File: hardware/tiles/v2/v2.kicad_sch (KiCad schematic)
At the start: 24 parts, among them J1 Conn_01x05_Pin, J2 Conn_01x05_Pin, J3 Conn_01x05_Pin, J4 Conn_01x05_Pin, J5 Conn_01x05_Pin, J6 Conn_01x05_Pin, J7 Conn_01x05_Pin, J8 Conn_01x05_Pin, J9 Conn_01x06_Pin, SW1 SW_DIP_x01, U1 ATmega328P-A, U2 DRV5055A2xDBZxQ1, Y2 Crystal_GND24

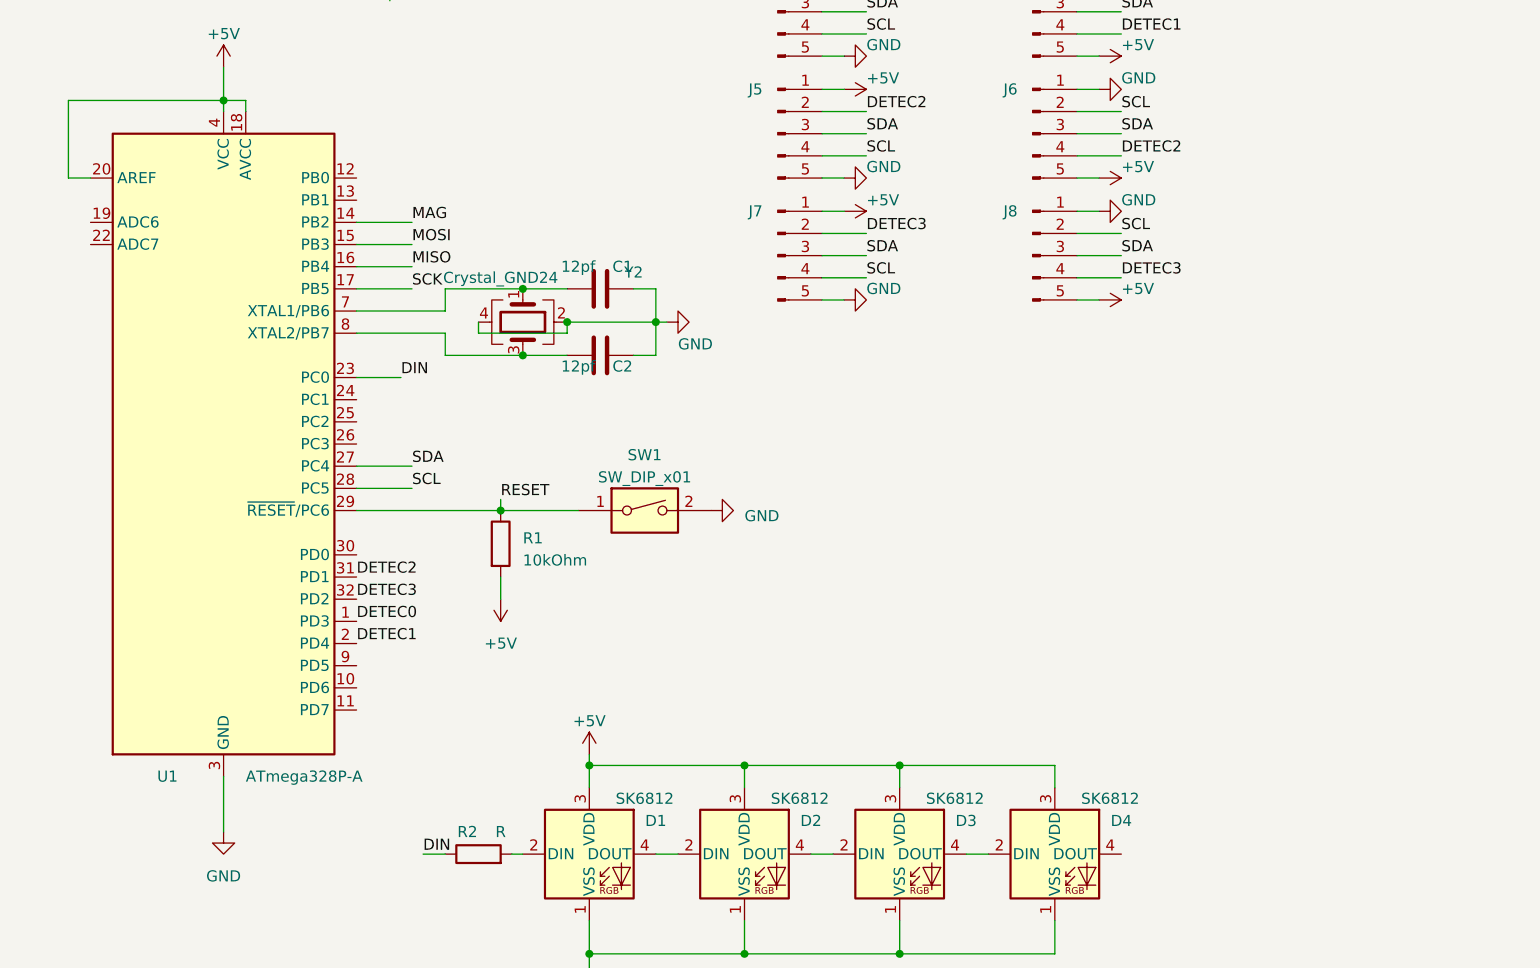
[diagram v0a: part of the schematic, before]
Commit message: Updating PCB with Capacitive touch and Color sensor
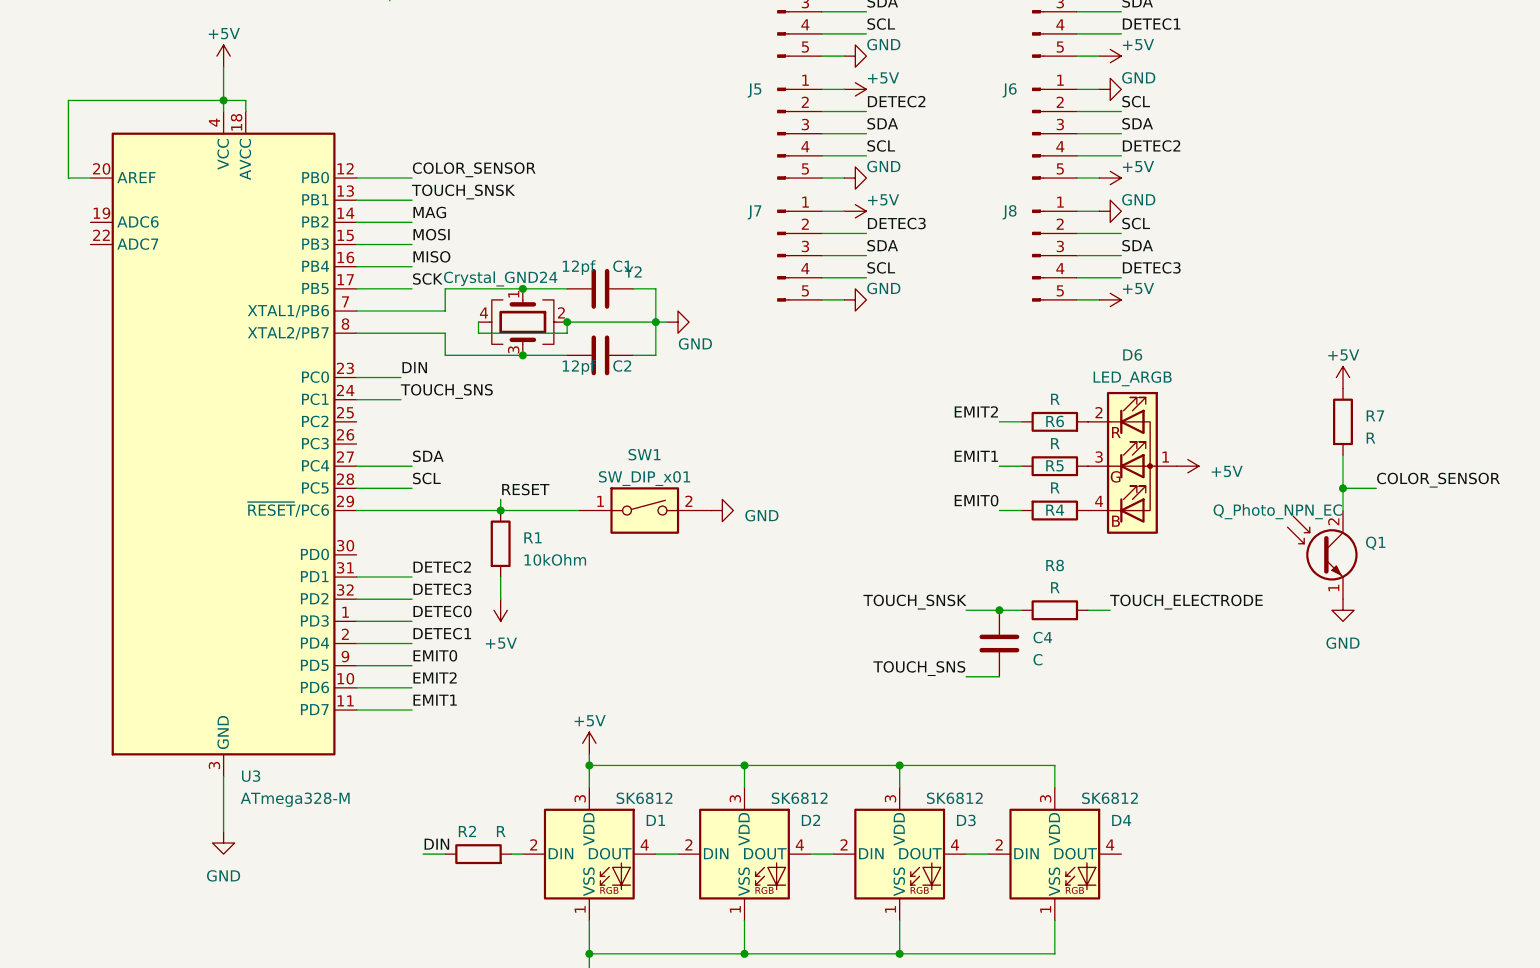
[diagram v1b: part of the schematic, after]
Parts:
- removed U1: ATmega328P-A, Package_QFP:TQFP-32_7x7mm_P0.8mm, symbol MCU_Microchip_ATmega:ATmega328P-A
- added C4: C, Capacitor_SMD:C_0402_1005Metric_Pad0.74x0.62mm_HandSolder, symbol Device:C
- added D6: LED_ARGB, LED_SMD:LED_WS2812B-2020_PLCC4_2.0x2.0mm, symbol Device:LED_ARGB
- added Q1: Q_Photo_NPN_EC, Resistor_SMD:R_0603_1608Metric_Pad0.98x0.95mm_HandSolder, symbol Device:Q_Photo_NPN_EC
- added R4, R5, R6, R7, R8: R, Resistor_SMD:R_0603_1608Metric_Pad0.98x0.95mm_HandSolder, symbol Device:R
- added U3: ATmega328-M, Package_DFN_QFN:QFN-32-1EP_5x5mm_P0.5mm_EP3.1x3.1mm, symbol MCU_Microchip_ATmega:ATmega328-M
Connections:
- net +5V: now also D6.1 (A), R7.1, U3.18 (AVCC), U3.20 (AREF), U3.4 (VCC), U3.6 (VCC)
- net DETEC0: now also U3.1 (PD3)
- net DETEC1: now also U3.2 (PD4)
- net DETEC2: now also U3.31 (PD1)
- net DETEC3: now also U3.32 (PD2)
- net DIN: now also U3.23 (PC0)
- net GND: now also Q1.1 (E), U3.21 (GND), U3.3 (GND), U3.33 (GND), U3.5 (GND)
- net MAG: now also U3.14 (PB2)
- net MISO: now also U3.16 (PB4)
- net MOSI: now also U3.15 (PB3)
- net RESET: now also U3.29 (~{RESET}/PC6)
- net SCK: now also U3.17 (PB5)
- net SCL: now also U3.28 (PC5)
- net SDA: now also U3.27 (PC4)
- net at C1.1, Y2.1: now also U3.7 (XTAL1/PB6)
- net at C2.1, Y2.3: now also U3.8 (XTAL2/PB7)
- new net: D6.2 (RK), R6.2
- new net: D6.3 (GK), R5.2
- new net: D6.4 (BK), R4.1
- new net COLOR_SENSOR: Q1.2 (C), R7.2, U3.12 (PB0)
- new net EMIT0: R4.2, U3.9 (PD5)
- new net EMIT1: R5.1, U3.11 (PD7)
- new net EMIT2: R6.1, U3.10 (PD6)
- new net TOUCH_ELECTRODE: R8.2
- new net TOUCH_SNS: C4.2, U3.24 (PC1)
- new net TOUCH_SNSK: C4.1, R8.1, U3.13 (PB1)

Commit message: Last atmega238 update
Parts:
- SW1: footprint Button_Switch_SMD:SW_SPST_PTS645 -> Button_Switch_SMD:SW_Push_1P1T_XKB_TS-1187A
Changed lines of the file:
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@@
       (effects (font (size 1.27 1.27)))
     )
-    (property "Footprint" "Button_Switch_SMD:SW_SPST_PTS645" (at 168.91 99.06 0)
+    (property "Footprint" "Button_Switch_SMD:SW_Push_1P1T_XKB_TS-1187A" (at 168.91 99.06 0)
       (effects (font (size 1.27 1.27)) hide)
     )

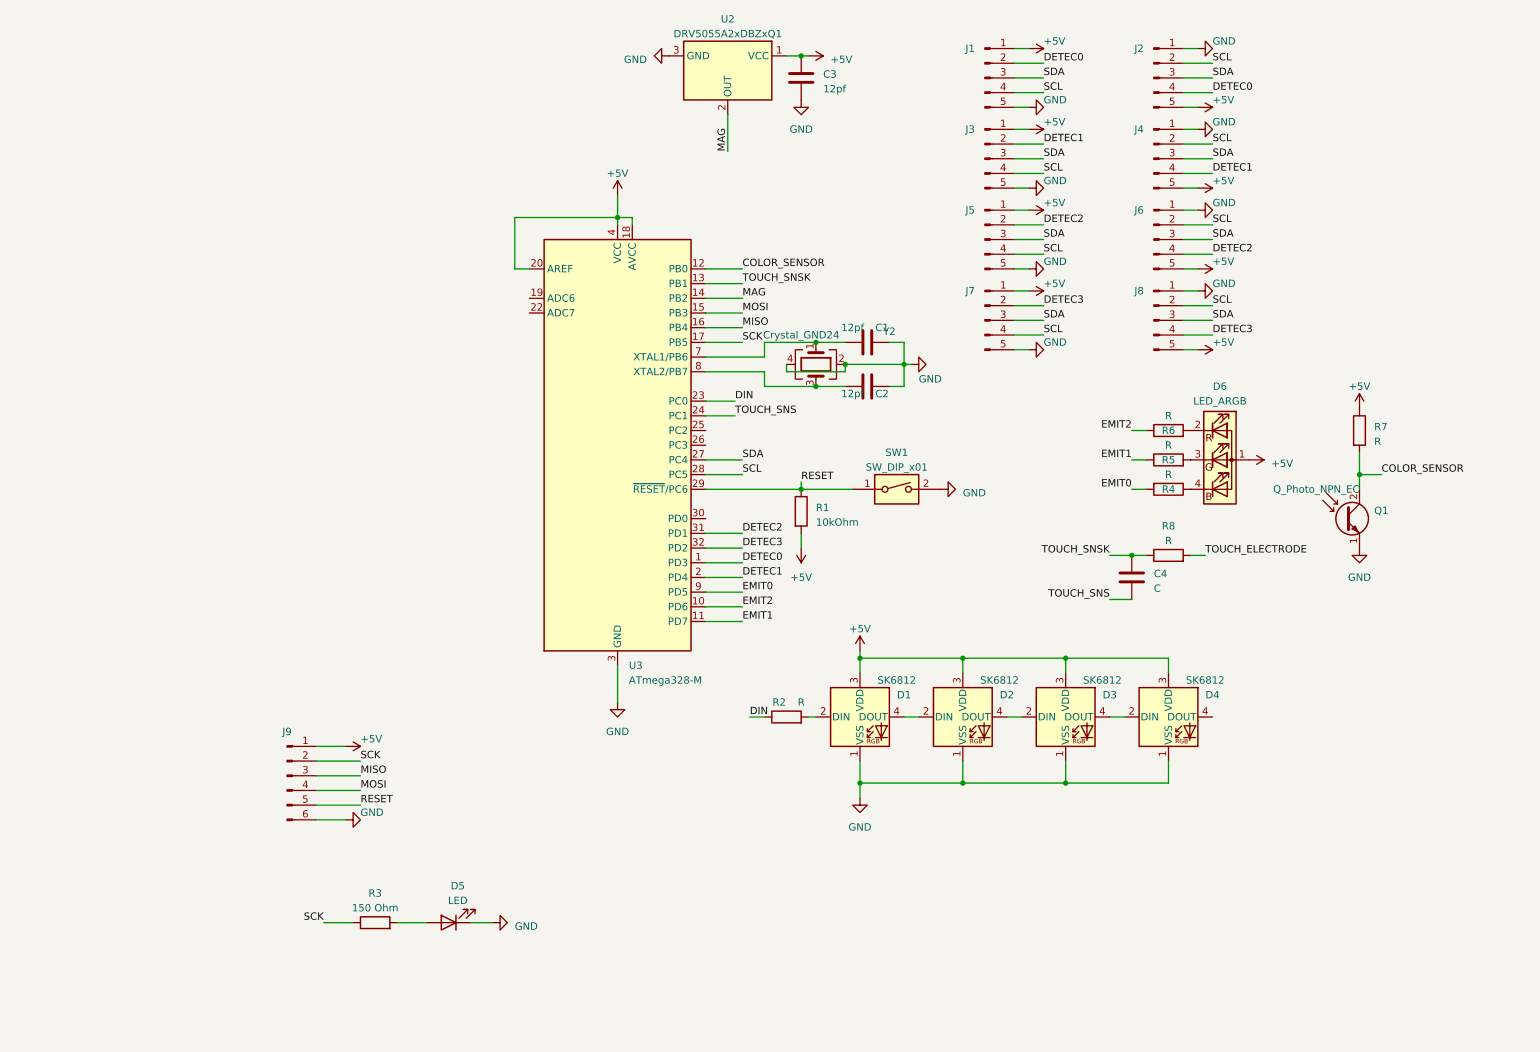
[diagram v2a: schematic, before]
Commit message: Updating pcb to support U-shaped pin connection, adding AREF decoupler
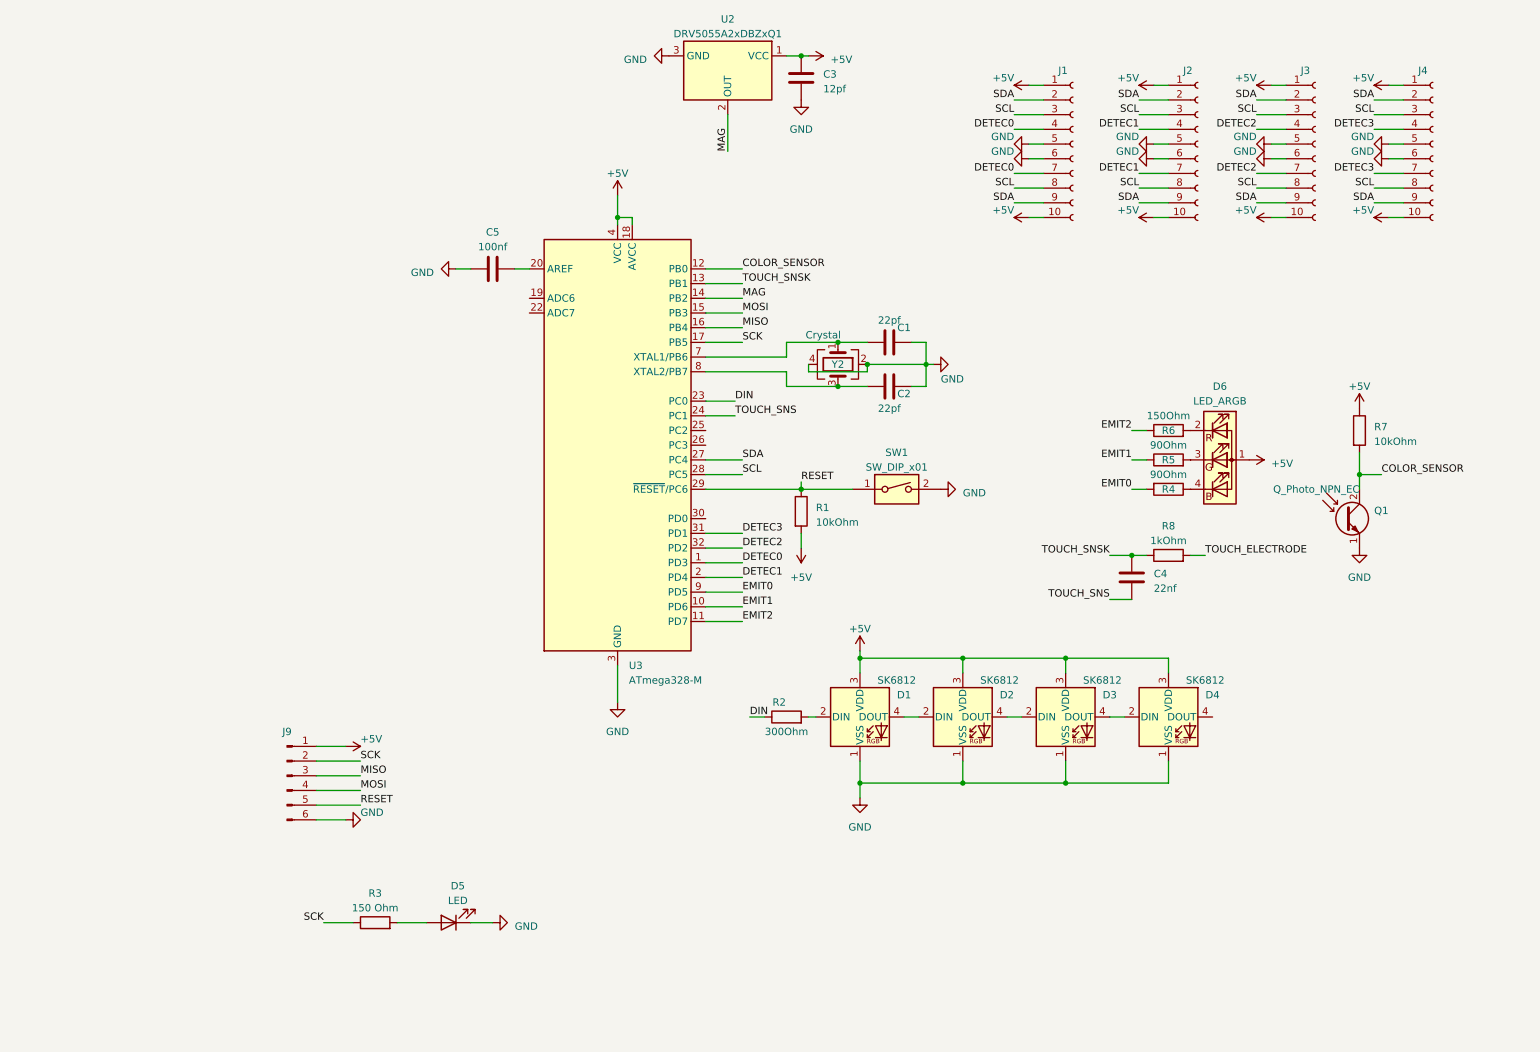
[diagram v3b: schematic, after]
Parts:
- removed J1, J2, J3, J4, J5, J6, J7, J8: Conn_01x05_Pin, Connector_PinHeader_2.54mm:PinHeader_1x05_P2.54mm_Horizontal, symbol Connector:Conn_01x05_Pin
- added C5: 100nf, Capacitor_SMD:C_0603_1608Metric_Pad1.08x0.95mm_HandSolder, symbol Device:C
- added J1, J2, J3, J4: Conn_01x10_Socket, Connector_PinSocket_2.54mm:PinSocket_1x10_P2.54mm_Vertical, symbol Connector:Conn_01x10_Socket
- C1, C2: value 12pf -> 22pf
- C4: value C -> 22nf
- R2: value R -> 300Ohm
- R4, R5: value R -> 90Ohm
- R6: value R -> 150Ohm
- R7: value R -> 10kOhm
- R8: value R -> 1kOhm
- Y2: value Crystal_GND24 -> Crystal
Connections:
- net +5V: now also J1.1 (Pin_1), J1.10 (Pin_10), J2.1 (Pin_1), J2.10 (Pin_10), J3.1 (Pin_1), J3.10 (Pin_10), J4.1 (Pin_1), J4.10 (Pin_10); no longer U3.20 (AREF)
- net DETEC0: now also J1.4 (Pin_4), J1.7 (Pin_7)
- net DETEC1: now also J2.4 (Pin_4), J2.7 (Pin_7)
- net DETEC2: now also U3.32 (PD2), J3.4 (Pin_4), J3.7 (Pin_7); no longer U3.31 (PD1)
- net DETEC3: now also U3.31 (PD1), J4.4 (Pin_4), J4.7 (Pin_7); no longer U3.32 (PD2)
- net EMIT1: now also U3.10 (PD6); no longer U3.11 (PD7)
- net EMIT2: now also U3.11 (PD7); no longer U3.10 (PD6)
- net GND: now also C5.1, J1.5 (Pin_5), J1.6 (Pin_6), J2.5 (Pin_5), J2.6 (Pin_6), J3.5 (Pin_5), J3.6 (Pin_6), J4.5 (Pin_5), J4.6 (Pin_6)
- net SCL: now also J1.3 (Pin_3), J1.8 (Pin_8), J2.3 (Pin_3), J2.8 (Pin_8), J3.3 (Pin_3), J3.8 (Pin_8), J4.3 (Pin_3), J4.8 (Pin_8)
- net SDA: now also J1.2 (Pin_2), J1.9 (Pin_9), J2.2 (Pin_2), J2.9 (Pin_9), J3.2 (Pin_2), J3.9 (Pin_9), J4.2 (Pin_2), J4.9 (Pin_9)
- new net: C5.2, U3.20 (AREF)
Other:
- moved on the sheet: C1, C2, Y2

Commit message: Quick save
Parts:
- removed C5: 100nf, Capacitor_SMD:C_0603_1608Metric_Pad1.08x0.95mm_HandSolder, symbol Device:C
- removed D6: LED_ARGB, LED_SMD:LED_WS2812B-2020_PLCC4_2.0x2.0mm, symbol Device:LED_ARGB
- removed J9: Conn_01x06_Pin, Connector_PinHeader_2.54mm:PinHeader_1x06_P2.54mm_Vertical, symbol Connector:Conn_01x06_Pin
- removed R4, R5: 90Ohm, Resistor_SMD:R_0603_1608Metric_Pad0.98x0.95mm_HandSolder, symbol Device:R
- removed R6: 150Ohm, Resistor_SMD:R_0603_1608Metric_Pad0.98x0.95mm_HandSolder, symbol Device:R
- removed R8: 1kOhm, Resistor_SMD:R_0603_1608Metric_Pad0.98x0.95mm_HandSolder, symbol Device:R
- removed U3: ATmega328-M, Package_DFN_QFN:QFN-32-1EP_5x5mm_P0.5mm_EP3.1x3.1mm, symbol MCU_Microchip_ATmega:ATmega328-M
- removed Y2: Crystal, Crystal:Crystal_SMD_3225-4Pin_3.2x2.5mm_HandSoldering, symbol Device:Crystal_GND24
- added C6: 1 uF, Capacitor_SMD:C_0603_1608Metric_Pad1.08x0.95mm_HandSolder, symbol Device:C
- added D7: SK6812, LED_SMD:LED_SK6812_PLCC4_5.0x5.0mm_P3.2mm, symbol LED:SK6812
- added J5: Conn_01x05_Socket, Connector_PinSocket_2.54mm:PinSocket_1x05_P2.54mm_Vertical, symbol Connector:Conn_01x05_Socket
- added SW2: SW_DIP_x01, Button_Switch_SMD:SW_Push_1P1T_XKB_TS-1187A, symbol Switch:SW_DIP_x01
- added U1: ESP32-S3-MINI-1, custom:ESP32-S3-MINI-1U, symbol Espressif:ESP32-S3-MINI-1
- added U3: AP7362A-33SP-13, custom:SOIC127P600X163-9N, symbol AP7362A:AP7362A-33SP-13
- C1: value 22pf -> 1 u; footprint Capacitor_SMD:C_0603_1608Metric_Pad1.08x0.95mm_HandSolder -> Capacitor_SMD:C_0603_1608Metric
- C2: value 22pf -> 1 uF
- C4: value 22nf -> 0.1 u; footprint Capacitor_SMD:C_0402_1005Metric_Pad0.74x0.62mm_HandSolder -> Capacitor_SMD:C_0603_1608Metric
- R1: value 10kOhm -> 10k; footprint Resistor_SMD:R_0603_1608Metric_Pad0.98x0.95mm_HandSolder -> Resistor_SMD:R_0603_1608Metric
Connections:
- net TOUCH_SNS is gone; now on net GND: C4.2
- net TOUCH_SNSK is gone; now on net EN: C4.1
- net +5V: now also C2.1, D7.3 (VDD), J5.4 (Pin_4), U3.2 (EN), U3.3 (IN), U3.4 (IN); no longer R1.2, R7.1
- net GND: now also C6.2, D7.1 (VSS), J5.1 (Pin_1), SW2.2, U1.1 (GND), U1.2 (GND), U1.42 (GND), U1.43 (GND), U1.46 (GND), U1.47 (GND), U1.48 (GND), U1.49 (GND), U1.50 (GND), U1.51 (GND), U1.52 (GND), U1.53 (GND), U1.54 (GND), U1.55 (GND), U1.56 (GND), U1.57 (GND), U1.58 (GND), U1.59 (GND), U1.60 (GND), U1.61 (GND), U1.62 (GND), U1.63 (GND), U1.64 (GND), U1.65 (GND), U3.1 (GND)
- net MISO: now also J5.2 (Pin_2)
- net RESET: now also J5.5 (Pin_5); no longer R1.1, SW1.1
- net SCK: now also J5.3 (Pin_3); no longer R3.1
- net EN: now reaches C1.1
- net EN: now also R1.2, SW1.1
- net at R2.2: now also D7.2 (DIN); no longer D1.2 (DIN)
- new net: D1.2 (DIN), D7.4 (DOUT)
- new net +3V3: C6.1, R1.1, R7.1, U1.3 (3V3), U3.5 (OUT), U3.6 (OUT), U3.7 (OUT)
- new net BOOT: SW2.1
- new net RX: R3.1
- new net TOUCH: U1.10 (GPIO6/TOUCH6/ADC1_CH5)
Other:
- note added: "3v3 ldo"
- note added: "Boot"
- note added: "Conn"
- note added: "Mag"
- note added: "Neopixels"
- note added: "Prog"
- note added: "Reset"
- moved on the sheet: C3, D1, D2, D3, D4, D5, J1, J2, J3, J4, Q1, R2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
